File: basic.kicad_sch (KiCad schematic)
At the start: 3 parts

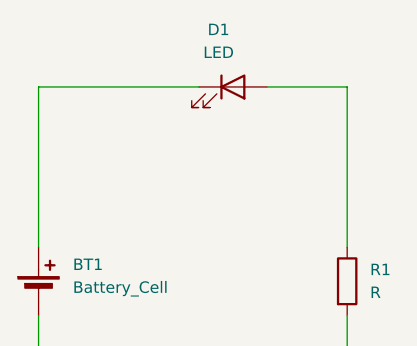
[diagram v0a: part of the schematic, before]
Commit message: added 1 led in series
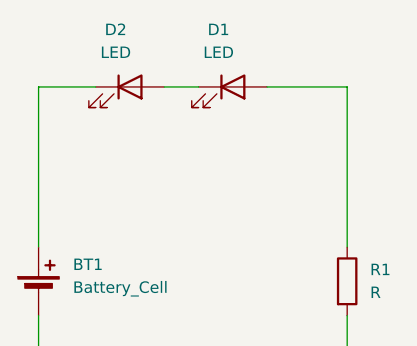
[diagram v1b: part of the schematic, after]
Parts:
- added D2: LED, symbol Device:LED
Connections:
- net at D1.1 (K): now also D2.2 (A); no longer BT1.1 (+)
- new net: BT1.1 (+), D2.1 (K)
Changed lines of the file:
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@@
+	(wire
+		(pts
+			(xy 87.63 85.09) (xy 93.98 85.09)
+		)
+		(stroke
+			(width 0)
+			(type default)
+		)
+	)
+	(wire
+		(pts
+			(xy 101.6 85.09) (xy 105.41 85.09)
+		)
+		(stroke
+			(width 0)
+			(type default)
+		)
+	)
 	(wire
 		(pts
@@
 		(pts
 			(xy 113.03 85.09) (xy 121.92 85.09)
-		)
-		(stroke
-			(width 0)
-			(type default)
-		)
-	)
-	(wire
-		(pts
-			(xy 87.63 85.09) (xy 105.41 85.09)
 		)
 		(stroke
@@
 					(unit 1)
 				)
+			)
+		)
+	)
+	(symbol
+		(lib_id "Device:LED")
+		(at 97.79 85.09 0)
+		(unit 1)
+		(exclude_from_sim no)
+		(in_bom yes)
+		(on_board yes)
+		(dnp no)
+		(fields_autoplaced yes)
+		(property "Reference" "D2"
+			(at 96.2025 78.74 0)
+			(effects
+				(font
+					(size 1.27 1.27)
+				)
+			)
+		)
+		(property "Value" "LED"
+			(at 96.2025 81.28 0)
+			(effects
+				(font
+					(size 1.27 1.27)
+				)
+			)
+		)
+		(property "Footprint" ""
+			(at 97.79 85.09 0)
+			(effects
+				(font
+					(size 1.27 1.27)
+				)
+				(hide yes)
+			)
+		)
+		(property "Datasheet" "~"
+			(at 97.79 85.09 0)
+			(effects
+				(font
+					(size 1.27 1.27)
+				)
+				(hide yes)
+			)
+		)
+		(property "Description" "Light emitting diode"
+			(at 97.79 85.09 0)
+			(effects
+				(font
+					(size 1.27 1.27)
+				)
+				(hide yes)
+			)
+		)
+		(property "Sim.Pins" "1=K 2=A"
+			(at 97.79 85.09 0)
+			(effects
+				(font
+					(size 1.27 1.27)
+				)
+				(hide yes)
+			)
+		)
+		(pin "2"
+		)
+		(pin "1"
+		)
+		(instances
+			(project "basic"
+				(path "/843f161b-4419-4ad9-a4d0-822448de2c5a"
+					(reference "D2")
+					(unit 1)
+				)

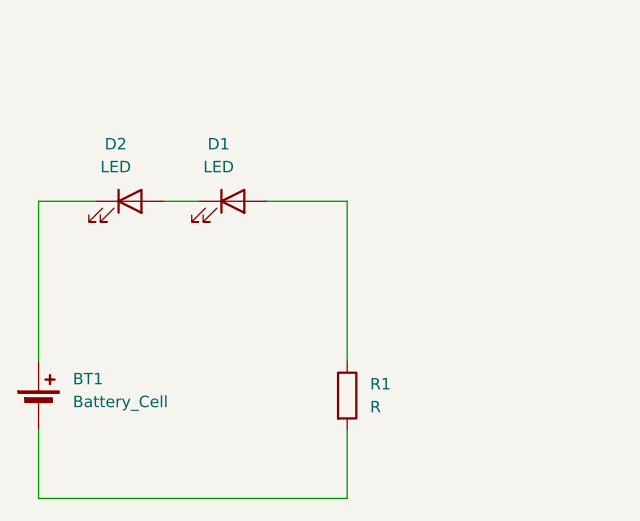
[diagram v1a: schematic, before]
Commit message: added 2 led in parallel
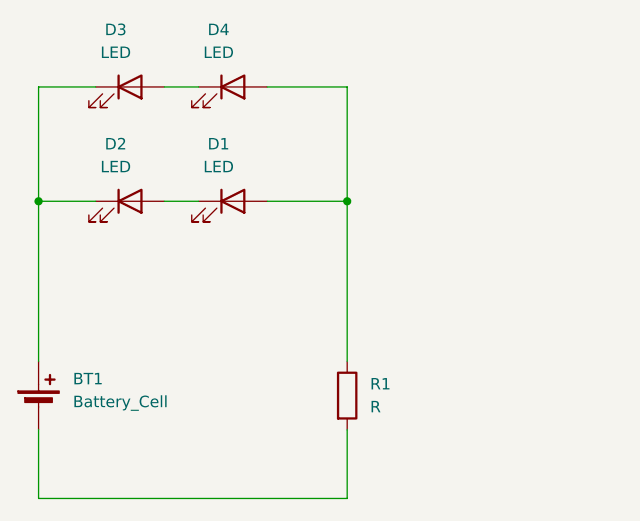
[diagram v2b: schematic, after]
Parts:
- added D3, D4: LED, symbol Device:LED
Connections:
- net at D1.2 (A), R1.1: now also D4.2 (A)
- net at BT1.1 (+), D2.1 (K): now also D3.1 (K)
- new net: D3.2 (A), D4.1 (K)
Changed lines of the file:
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@@
 	(generator_version "9.0")
 	(paper "A4")
+	(junction
+		(at 121.92 85.09)
+		(diameter 0)
+		(color 0 0 0 0)
+	)
+	(junction
+		(at 87.63 85.09)
+		(diameter 0)
+		(color 0 0 0 0)
+	)
 	(wire
 		(pts
@@
 	(wire
 		(pts
+			(xy 93.98 72.39) (xy 87.63 72.39)
+		)
+		(stroke
+			(width 0)
+			(type default)
+		)
+	)
+	(wire
+		(pts
 			(xy 113.03 85.09) (xy 121.92 85.09)
 		)
@@
 		(pts
 			(xy 121.92 85.09) (xy 121.92 102.87)
+		)
+		(stroke
+			(width 0)
+			(type default)
+		)
+	)
+	(wire
+		(pts
+			(xy 113.03 72.39) (xy 121.92 72.39)
+		)
+		(stroke
+			(width 0)
+			(type default)
+		)
+	)
+	(wire
+		(pts
+			(xy 121.92 72.39) (xy 121.92 85.09)
+		)
+		(stroke
+			(width 0)
+			(type default)
+		)
+	)
+	(wire
+		(pts
+			(xy 87.63 72.39) (xy 87.63 85.09)
+		)
+		(stroke
+			(width 0)
+			(type default)
+		)
+	)
+	(wire
+		(pts
+			(xy 101.6 72.39) (xy 105.41 72.39)
 		)
 		(stroke
@@
 					(unit 1)
 				)
+			)
+		)
+	)
+	(symbol
+		(lib_id "Device:LED")
+		(at 97.79 72.39 0)
+		(unit 1)
+		(exclude_from_sim no)
+		(in_bom yes)
+		(on_board yes)
+		(dnp no)
+		(fields_autoplaced yes)
+		(property "Reference" "D3"
+			(at 96.2025 66.04 0)
+			(effects
+				(font
+					(size 1.27 1.27)
+				)
+			)
+		)
+		(property "Value" "LED"
+			(at 96.2025 68.58 0)
+			(effects
+				(font
+					(size 1.27 1.27)
+				)
+			)
+		)
+		(property "Footprint" ""
+			(at 97.79 72.39 0)
+			(effects
+				(font
+					(size 1.27 1.27)
+				)
+				(hide yes)
+			)
+		)
+		(property "Datasheet" "~"
+			(at 97.79 72.39 0)
+			(effects
+				(font
+					(size 1.27 1.27)
+				)
+				(hide yes)
+			)
+		)
+		(property "Description" "Light emitting diode"
+			(at 97.79 72.39 0)
+			(effects
+				(font
+					(size 1.27 1.27)
+				)
+				(hide yes)
+			)
+		)
+		(property "Sim.Pins" "1=K 2=A"
+			(at 97.79 72.39 0)
+			(effects
+				(font
+					(size 1.27 1.27)
+				)
+				(hide yes)
+			)
+		)
+		(pin "2"
+		)
+		(pin "1"
+		)
+		(instances
+			(project "basic"
+				(path "/843f161b-4419-4ad9-a4d0-822448de2c5a"
+					(reference "D3")
+					(unit 1)
+				)
+			)
+		)
+	)
+	(symbol
+		(lib_id "Device:LED")
+		(at 109.22 72.39 0)
+		(unit 1)
+		(exclude_from_sim no)
+		(in_bom yes)
+		(on_board yes)
+		(dnp no)
+		(fields_autoplaced yes)
+		(property "Reference" "D4"
+			(at 107.6325 66.04 0)
+			(effects
+				(font
+					(size 1.27 1.27)
+				)
+			)
+		)
+		(property "Value" "LED"
+			(at 107.6325 68.58 0)
+			(effects
+				(font
+					(size 1.27 1.27)
+				)
+			)
+		)
+		(property "Footprint" ""
+			(at 109.22 72.39 0)
+			(effects
+				(font
+					(size 1.27 1.27)
+				)
+				(hide yes)
+			)
+		)
+		(property "Datasheet" "~"
+			(at 109.22 72.39 0)
+			(effects
+				(font
+					(size 1.27 1.27)
+				)
+				(hide yes)
+			)
+		)
+		(property "Description" "Light emitting diode"
+			(at 109.22 72.39 0)
+			(effects
+				(font
+					(size 1.27 1.27)
+				)
+				(hide yes)
+			)
+		)
+		(property "Sim.Pins" "1=K 2=A"
+			(at 109.22 72.39 0)
+			(effects
+				(font
+					(size 1.27 1.27)
+				)
+				(hide yes)
+			)
+		)
+		(pin "2"
+		)
+		(pin "1"
+		)
+		(instances
+			(project "basic"
+				(path "/843f161b-4419-4ad9-a4d0-822448de2c5a"
+					(reference "D4")
+					(unit 1)
+				)

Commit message: added buzzer
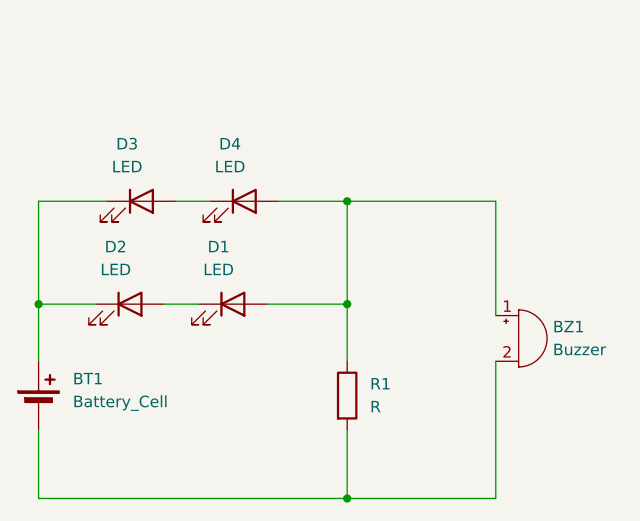
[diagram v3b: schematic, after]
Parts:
- added BZ1: Buzzer, symbol Device:Buzzer
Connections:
- net at D1.2 (A), D4.2 (A), R1.1: now also BZ1.1 (+)
- net at BT1.2 (-), R1.2: now also BZ1.2 (-)
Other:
- moved on the sheet: D1, D2, D3, D4
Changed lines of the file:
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@@
 	(paper "A4")
+	(junction
+		(at 87.63 96.52)
+		(diameter 0)
+		(color 0 0 0 0)
+	)
 	(junction
 		(at 121.92 85.09)
@@
 	)
 	(junction
-		(at 87.63 85.09)
+		(at 121.92 118.11)
 		(diameter 0)
 		(color 0 0 0 0)
 	)
-	(wire
-		(pts
-			(xy 87.63 85.09) (xy 93.98 85.09)
-		)
-		(stroke
-			(width 0)
-			(type default)
-		)
-	)
-	(wire
-		(pts
-			(xy 101.6 85.09) (xy 105.41 85.09)
+	(junction
+		(at 121.92 96.52)
+		(diameter 0)
+		(color 0 0 0 0)
+	)
+	(wire
+		(pts
+			(xy 87.63 85.09) (xy 87.63 96.52)
+		)
+		(stroke
+			(width 0)
+			(type default)
+		)
+	)
+	(wire
+		(pts
+			(xy 121.92 96.52) (xy 121.92 102.87)
+		)
+		(stroke
+			(width 0)
+			(type default)
+		)
+	)
+	(wire
+		(pts
+			(xy 138.43 118.11) (xy 121.92 118.11)
+		)
+		(stroke
+			(width 0)
+			(type default)
+		)
+	)
+	(wire
+		(pts
+			(xy 87.63 96.52) (xy 93.98 96.52)
+		)
+		(stroke
+			(width 0)
+			(type default)
+		)
+	)
+	(wire
+		(pts
+			(xy 138.43 85.09) (xy 121.92 85.09)
+		)
+		(stroke
+			(width 0)
+			(type default)
+		)
+	)
+	(wire
+		(pts
+			(xy 138.43 97.79) (xy 138.43 85.09)
+		)
+		(stroke
+			(width 0)
+			(type default)
+		)
+	)
+	(wire
+		(pts
+			(xy 101.6 96.52) (xy 105.41 96.52)
 		)
 		(stroke
@@
 	(wire
 		(pts
-			(xy 93.98 72.39) (xy 87.63 72.39)
-		)
-		(stroke
-			(width 0)
-			(type default)
-		)
-	)
-	(wire
-		(pts
-			(xy 113.03 85.09) (xy 121.92 85.09)
+			(xy 95.25 85.09) (xy 87.63 85.09)
+		)
+		(stroke
+			(width 0)
+			(type default)
+		)
+	)
+	(wire
+		(pts
+			(xy 113.03 96.52) (xy 121.92 96.52)
 		)
 		(stroke
@@
 	(wire
 		(pts
-			(xy 87.63 102.87) (xy 87.63 85.09)
-		)
-		(stroke
-			(width 0)
-			(type default)
-		)
-	)
-	(wire
-		(pts
-			(xy 121.92 85.09) (xy 121.92 102.87)
-		)
-		(stroke
-			(width 0)
-			(type default)
-		)
-	)
-	(wire
-		(pts
-			(xy 113.03 72.39) (xy 121.92 72.39)
-		)
-		(stroke
-			(width 0)
-			(type default)
-		)
-	)
-	(wire
-		(pts
-			(xy 121.92 72.39) (xy 121.92 85.09)
-		)
-		(stroke
-			(width 0)
-			(type default)
-		)
-	)
-	(wire
-		(pts
-			(xy 87.63 72.39) (xy 87.63 85.09)
-		)
-		(stroke
-			(width 0)
-			(type default)
-		)
-	)
-	(wire
-		(pts
-			(xy 101.6 72.39) (xy 105.41 72.39)
+			(xy 87.63 102.87) (xy 87.63 96.52)
+		)
+		(stroke
+			(width 0)
+			(type default)
+		)
+	)
+	(wire
+		(pts
+			(xy 121.92 85.09) (xy 121.92 96.52)
+		)
+		(stroke
+			(width 0)
+			(type default)
+		)
+	)
+	(wire
+		(pts
+			(xy 138.43 102.87) (xy 138.43 118.11)
+		)
+		(stroke
+			(width 0)
+			(type default)
+		)
+	)
+	(wire
+		(pts
+			(xy 114.3 85.09) (xy 121.92 85.09)
+		)
+		(stroke
+			(width 0)
+			(type default)
+		)
+	)
+	(wire
+		(pts
+			(xy 102.87 85.09) (xy 106.68 85.09)
 		)
 		(stroke
@@
 	(symbol
 		(lib_id "Device:LED")
-		(at 109.22 85.09 0)
+		(at 109.22 96.52 0)
 		(unit 1)
 		(exclude_from_sim no)
@@
 		(fields_autoplaced yes)
 		(property "Reference" "D1"
-			(at 107.6325 78.74 0)
+			(at 107.6325 90.17 0)
 			(effects
 				(font
@@
 		)
 		(property "Value" "LED"
-			(at 107.6325 81.28 0)
+			(at 107.6325 92.71 0)
 			(effects
 				(font
@@
 		)
 		(property "Footprint" ""
-			(at 109.22 85.09 0)
+			(at 109.22 96.52 0)
 			(effects
 				(font
@@
 		)
 		(property "Datasheet" "~"
-			(at 109.22 85.09 0)
+			(at 109.22 96.52 0)
 			(effects
 				(font
@@
 		)
 		(property "Description" "Light emitting diode"
-			(at 109.22 85.09 0)
+			(at 109.22 96.52 0)
 			(effects
 				(font
@@
 		)
 		(property "Sim.Pins" "1=K 2=A"
-			(at 109.22 85.09 0)
+			(at 109.22 96.52 0)
 			(effects
 				(font
@@
 				(path "/843f161b-4419-4ad9-a4d0-822448de2c5a"
 					(reference "D1")
+					(unit 1)
+				)
+			)
+		)
+	)
+	(symbol
+		(lib_id "Device:Buzzer")
+		(at 140.97 100.33 0)
+		(unit 1)
+		(exclude_from_sim no)
+		(in_bom yes)
+		(on_board yes)
+		(dnp no)
+		(fields_autoplaced yes)
+		(property "Reference" "BZ1"
+			(at 144.78 99.0599 0)
+			(effects
+				(font
+					(size 1.27 1.27)
+				)
+				(justify left)
+			)
+		)
+		(property "Value" "Buzzer"
+			(at 144.78 101.5999 0)
+			(effects
+				(font
+					(size 1.27 1.27)
+				)
+				(justify left)
+			)
+		)
+		(property "Footprint" ""
+			(at 140.335 97.79 90)
+			(effects
+				(font
+					(size 1.27 1.27)
+				)
+				(hide yes)
+			)
+		)
+		(property "Datasheet" "~"
+			(at 140.335 97.79 90)
+			(effects
+				(font
+					(size 1.27 1.27)
+				)
+				(hide yes)
+			)
+		)
+		(property "Description" "Buzzer, polarized"
+			(at 140.97 100.33 0)
+			(effects
+				(font
+					(size 1.27 1.27)
+				)
+				(hide yes)
+			)
+		)
+		(pin "1"
+		)
+		(pin "2"
+		)
+		(instances
+			(project ""
+				(path "/843f161b-4419-4ad9-a4d0-822448de2c5a"
+					(reference "BZ1")
 					(unit 1)
 				)
@@
 	(symbol
 		(lib_id "Device:LED")
-		(at 97.79 72.39 0)
+		(at 99.06 85.09 0)
 		(unit 1)
 		(exclude_from_sim no)
@@
 		(fields_autoplaced yes)
 		(property "Reference" "D3"
-			(at 96.2025 66.04 0)
+			(at 97.4725 78.74 0)
 			(effects
 				(font
@@
 		)
 		(property "Value" "LED"
-			(at 96.2025 68.58 0)
+			(at 97.4725 81.28 0)
 			(effects
 				(font
@@
 		)
 		(property "Footprint" ""
-			(at 97.79 72.39 0)
+			(at 99.06 85.09 0)
 			(effects
 				(font
@@
 		)
 		(property "Datasheet" "~"
-			(at 97.79 72.39 0)
+			(at 99.06 85.09 0)
 			(effects
 				(font
@@
 		)
 		(property "Description" "Light emitting diode"
-			(at 97.79 72.39 0)
+			(at 99.06 85.09 0)
 			(effects
 				(font
@@
 		)
 		(property "Sim.Pins" "1=K 2=A"
-			(at 97.79 72.39 0)
+			(at 99.06 85.09 0)
 			(effects
 				(font
@@
 	(symbol
 		(lib_id "Device:LED")
-		(at 109.22 72.39 0)
+		(at 110.49 85.09 0)
 		(unit 1)
 		(exclude_from_sim no)
@@
 		(fields_autoplaced yes)
 		(property "Reference" "D4"
-			(at 107.6325 66.04 0)
+			(at 108.9025 78.74 0)
 			(effects
 				(font
@@
 		)
 		(property "Value" "LED"
-			(at 107.6325 68.58 0)
+			(at 108.9025 81.28 0)
 			(effects
 				(font
@@
 		)
 		(property "Footprint" ""
-			(at 109.22 72.39 0)
+			(at 110.49 85.09 0)
 			(effects
 				(font
@@
 		)
 		(property "Datasheet" "~"
-			(at 109.22 72.39 0)
+			(at 110.49 85.09 0)
 			(effects
 				(font
@@
 		)
 		(property "Description" "Light emitting diode"
-			(at 109.22 72.39 0)
+			(at 110.49 85.09 0)
 			(effects
 				(font
@@
 		)
 		(property "Sim.Pins" "1=K 2=A"
-			(at 109.22 72.39 0)
+			(at 110.49 85.09 0)
 			(effects
 				(font
@@
 	(symbol
 		(lib_id "Device:LED")
-		(at 97.79 85.09 0)
+		(at 97.79 96.52 0)
 		(unit 1)
 		(exclude_from_sim no)
@@
 		(fields_autoplaced yes)
 		(property "Reference" "D2"
-			(at 96.2025 78.74 0)
+			(at 96.2025 90.17 0)
 			(effects
 				(font
@@
 		)
 		(property "Value" "LED"
-			(at 96.2025 81.28 0)
+			(at 96.2025 92.71 0)
 			(effects
 				(font
@@
 		)
 		(property "Footprint" ""
-			(at 97.79 85.09 0)
+			(at 97.79 96.52 0)
 			(effects
 				(font
@@
 		)
 		(property "Datasheet" "~"
-			(at 97.79 85.09 0)
+			(at 97.79 96.52 0)
 			(effects
 				(font
@@
 		)
 		(property "Description" "Light emitting diode"
-			(at 97.79 85.09 0)
+			(at 97.79 96.52 0)
 			(effects
 				(font
@@
 		)
 		(property "Sim.Pins" "1=K 2=A"
-			(at 97.79 85.09 0)
-			(effects
-				(font
+			(at 97.79 96.52 0)
+			(effects
+				(font
